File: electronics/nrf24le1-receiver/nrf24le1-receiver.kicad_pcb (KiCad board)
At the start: 2 copper layers, 16 parts, among them K1 CONN_3, K2 CONN_3, K3 CONN_3, K4 CONN_3, SW1 SW_PUSH, U1 MCP1703T-3302E/CB, U2 NRF24LE1-MODULE-15X21

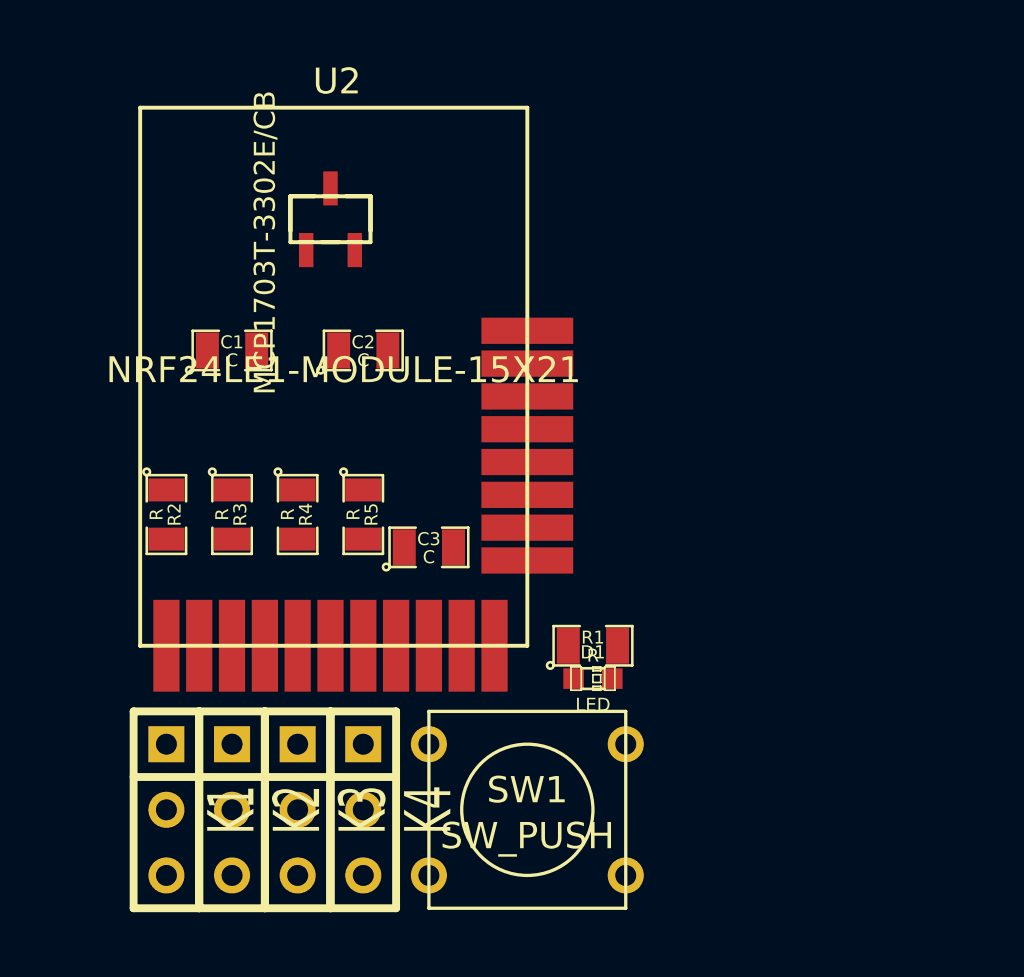
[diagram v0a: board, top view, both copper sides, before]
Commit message: Work on the layout of the NRF24LE1 receiver
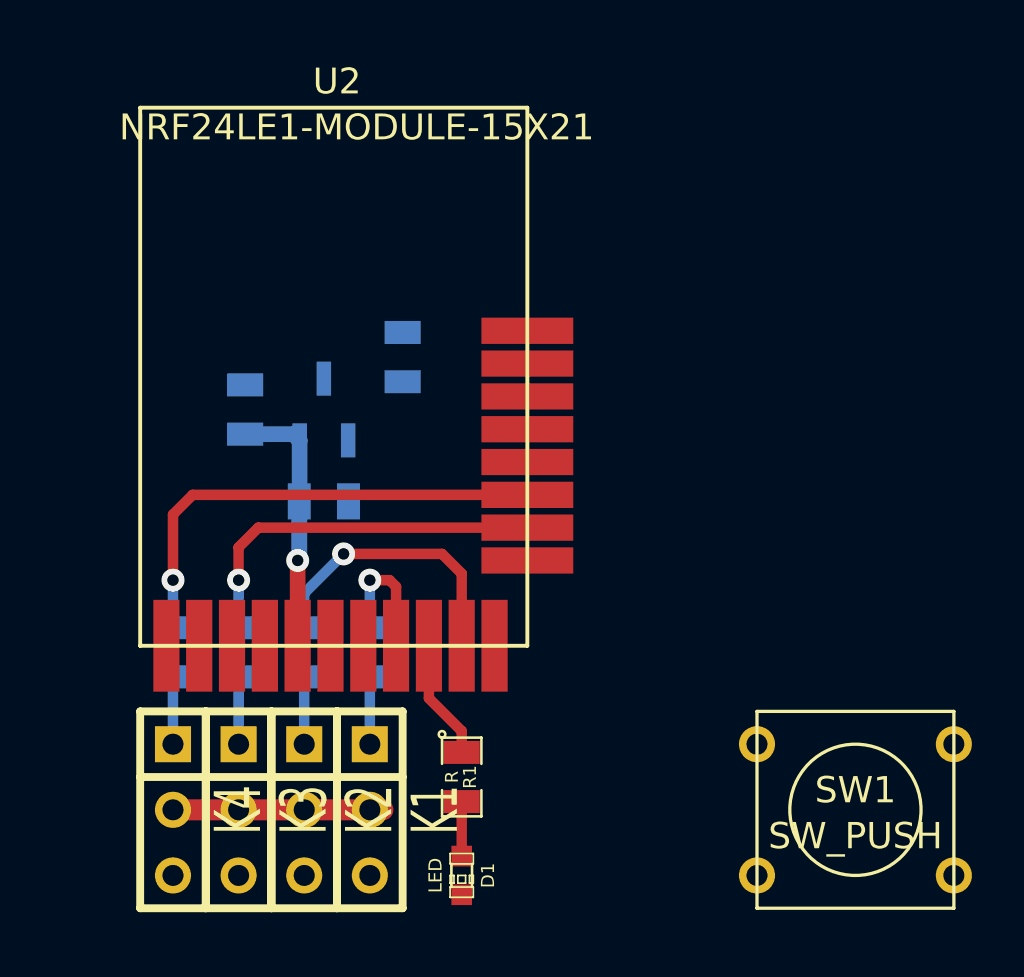
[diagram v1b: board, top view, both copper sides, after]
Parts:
- C1, C2, C3, R2, R3, R4, R5, U1: moved to B.Cu
- moved SW1 12.7 mm to (61.0, 68.6)
- moved R2 9.51 mm to (42.2, 62.5)
- moved D1 9.16 mm to (45.7, 71.1), turned to 270 degrees
- moved R5 9.09 mm to (34.5, 62.5)
- moved K1 7.87 mm to (42.2, 68.6)
- moved U1 7.37 mm to (40.4, 53.1), turned to 180 degrees
- moved K4 7.37 mm to (34.5, 68.6)
- moved R1 7.18 mm to (45.7, 67.3), turned to 270 degrees
- moved R3 6.02 mm to (39.6, 62.5)
- moved R4 5.80 mm to (37.1, 62.5)
- moved C3 4.44 mm to (40.4, 56.6)
- moved K2 2.79 mm to (39.6, 68.6)
- moved C1 2.34 mm to (37.3, 53.1), turned to 90 degrees
- moved K3 2.29 mm to (37.1, 68.6)
- moved C2 1.55 mm to (43.4, 51.1), turned to 90 degrees
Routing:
- net /MISO: track 0.00 -> 18.4 mm, vias 0 -> 1
- net /MOSI: track 0.00 -> 14.6 mm, vias 0 -> 1
- net /SCK: track 0.00 -> 11.2 mm, vias 0 -> 1
- net +3.3V: track 0.00 -> 10.2 mm, vias 0 -> 1
- net +BATT: track 0.00 -> 7.62 mm
- net /TX: track 0.00 -> 5.25 mm, vias 0 -> 1
- net /LED: track 0.00 -> 4.65 mm
- net N-0000017: track 0.00 -> 2.60 mm
- net N-0000016: track 0.00 -> 2.60 mm
- net N-0000015: track 0.00 -> 2.60 mm
- net N-0000014: track 0.00 -> 2.60 mm
- net N-000009: track 0.00 -> 2.11 mm
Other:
- net class Default: via_drill 0.635 -> 0.5
- rule trace_min: 0.254 -> 0.1524
- rule via_min_drill: 0.508 -> 0.3048
- rule via_min_size: 0.889 -> 0.6096

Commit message: Tweak schematics and layout
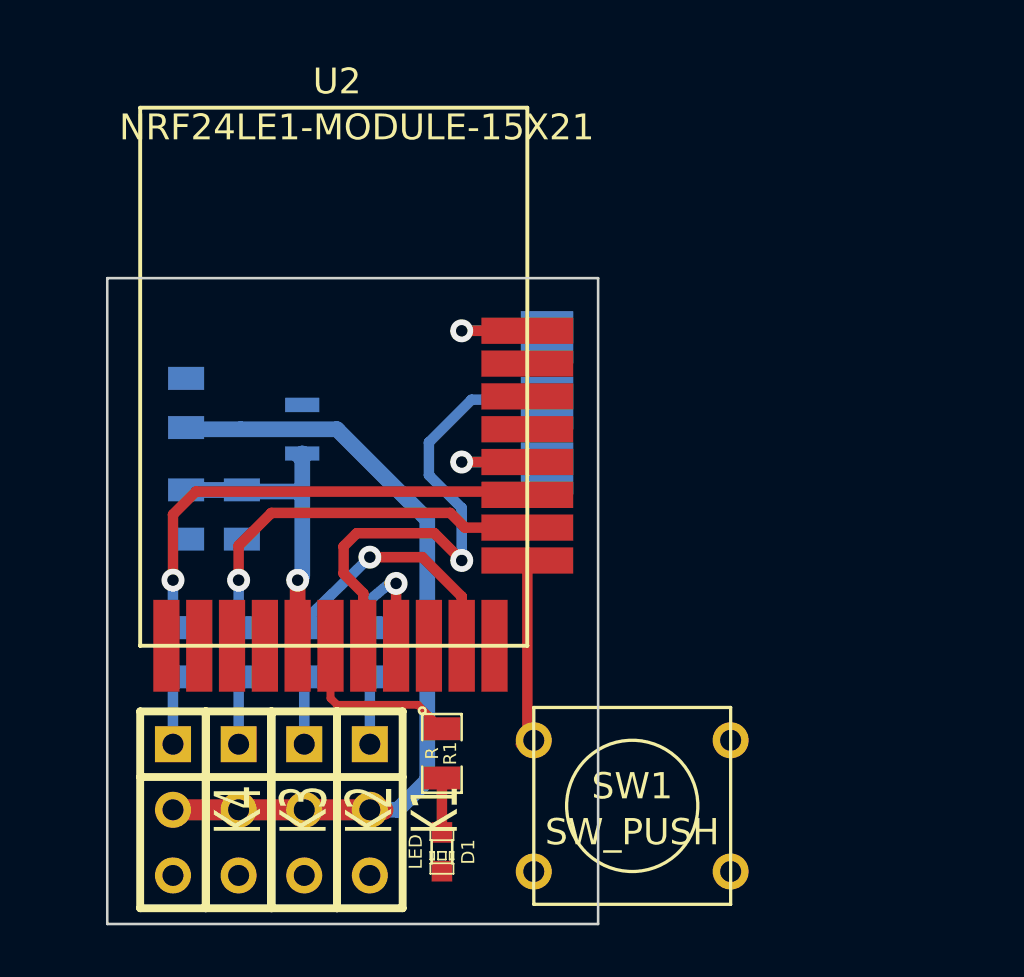
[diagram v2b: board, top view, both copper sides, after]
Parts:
- added P1: CONN_1, testpad_80mil_sq, B.Cu at (49.0, 52.8)
- added P2: CONN_1, testpad_80mil_sq, B.Cu at (49.0, 50.3)
- added P3: CONN_1, testpad_80mil_sq, B.Cu at (49.0, 55.4)
- moved SW1 8.64 mm to (52.3, 68.4)
- moved C2 8.57 mm to (35.1, 52.8)
- moved C1 4.66 mm to (35.1, 57.1), turned to 270 degrees
- moved C3 3.22 mm to (37.2, 57.1), turned to 270 degrees
- moved U1 2.17 mm to (38.4, 53.8), turned to 270 degrees
- moved D1 1.19 mm to (45.0, 70.2)
- moved R1 1.19 mm to (45.0, 66.4)
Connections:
- net /MISO renamed /CH1-MISO
- net /MOSI renamed /CH2-MOSI
- net /SCK renamed /CH3-SCK
- U2 pad 15: (no net) -> /CSN
- U2 pad 19: (no net) -> /RESET
- U2 pad 6: (no net) -> /LED
- U2 pad 7: (no net) -> /PROG
- U2 pad 9: /LED -> (no net)
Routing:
- net +BATT: track 7.62 -> 31.2 mm
- net /PROG: track 0.00 -> 19.0 mm, vias 0 -> 1
- net /BIND: track 0.00 -> 7.22 mm
- net /RESET: track 0.00 -> 5.13 mm, vias 0 -> 1
- net /CSN: track 0.00 -> 5.13 mm, vias 0 -> 1
- net /LED: track 4.65 -> 6.84 mm
- net +3.3V: track 10.2 -> 12.2 mm
- net /CH3-SCK: track 11.2 -> 9.89 mm
- net /CH2-MOSI: track 14.6 -> 15.1 mm
- added copper zone on B.Cu, net VSS
- added copper zone on F.Cu, net VSS
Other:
- board outline added: 19 x 25 mm

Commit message: Use round tact switch, tidy up the board
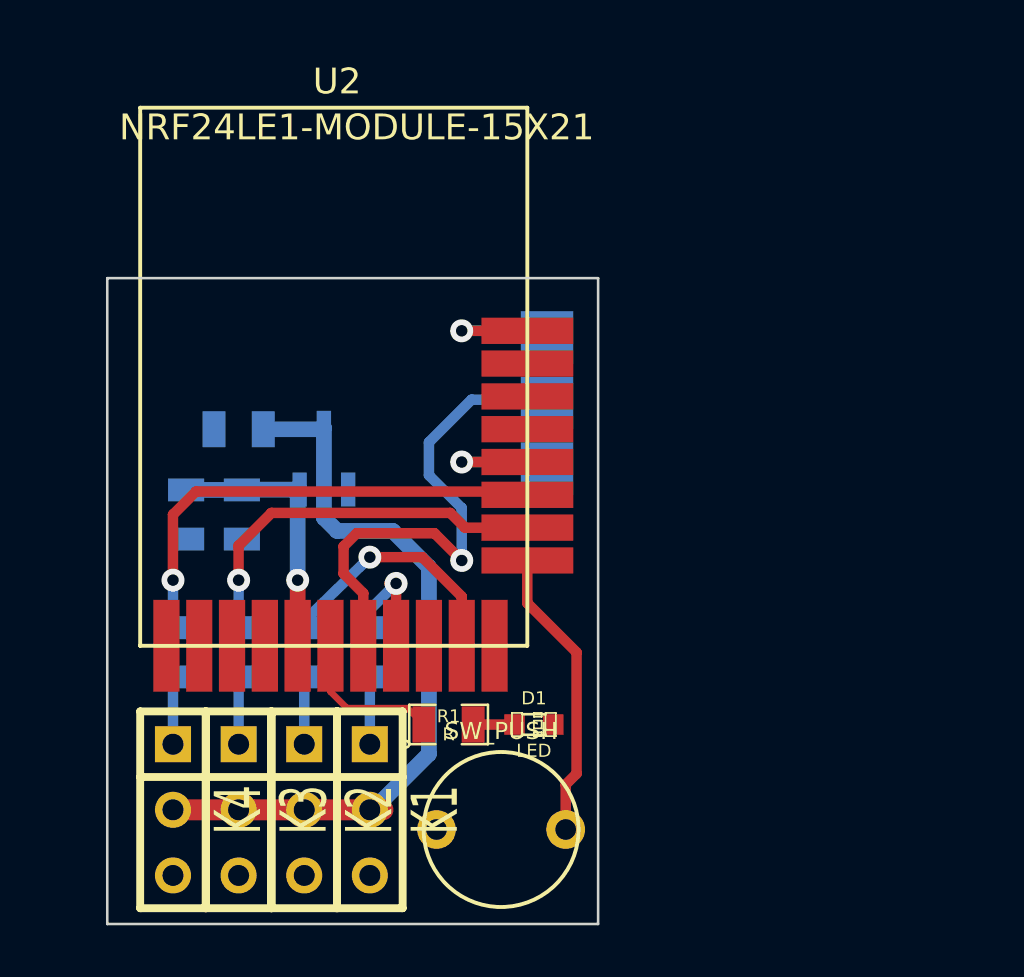
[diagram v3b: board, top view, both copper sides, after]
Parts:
- SW1: footprint SW_PUSH_SMALL -> SW_PUSH_ROUND_6mm
- moved D1 6.08 mm to (48.5, 65.3), turned to 0 degrees
- moved SW1 5.16 mm to (47.2, 69.3), turned to 180 degrees
- moved U1 2.33 mm to (40.4, 55.0), turned to 180 degrees
- moved C2 2.27 mm to (37.1, 53.8), turned to 180 degrees
- moved R1 1.15 mm to (45.2, 65.3), turned to 0 degrees
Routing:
- net /BIND: track 7.22 -> 11.4 mm
- net +BATT: track 31.2 -> 28.7 mm
- net +3.3V: track 12.2 -> 10.6 mm
- net /LED: track 6.84 -> 5.92 mm
- net N-000003: track 2.11 -> 1.60 mm

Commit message: Improve silk screen
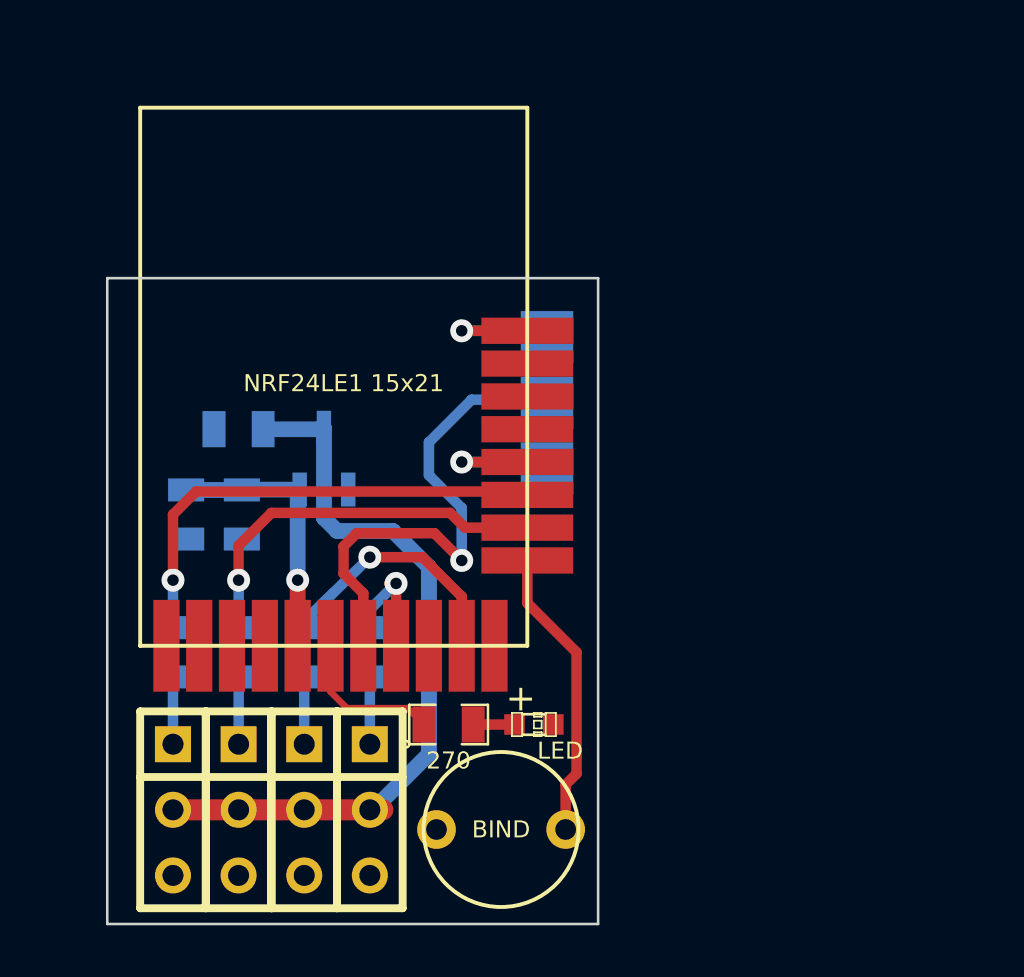
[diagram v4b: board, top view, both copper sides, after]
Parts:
- C1: value C -> 10u
- C2, C3: value C -> 1u
- R1: value R -> 270
- R2, R3, R4, R5: value R -> 820
- SW1: value SW_PUSH -> BIND
- U1: value MCP1703T-3302E/CB -> MCP1703
- U2: value NRF24LE1-MODULE-15X21 -> NRF24LE1 15x21
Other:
- board text added: "+"
- board text added: "CSN"
- board text added: "LANE Boys RC"
- board text added: "MISO"
- board text added: "MOSI"
- board text added: "NRF24LE1 receiver"
- board text added: "PROG"
- board text added: "RESET"
- board text added: "Rev 1"
- board text added: "SCK"
- board text added: "TX"

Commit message: Make pinout similar to XR3100
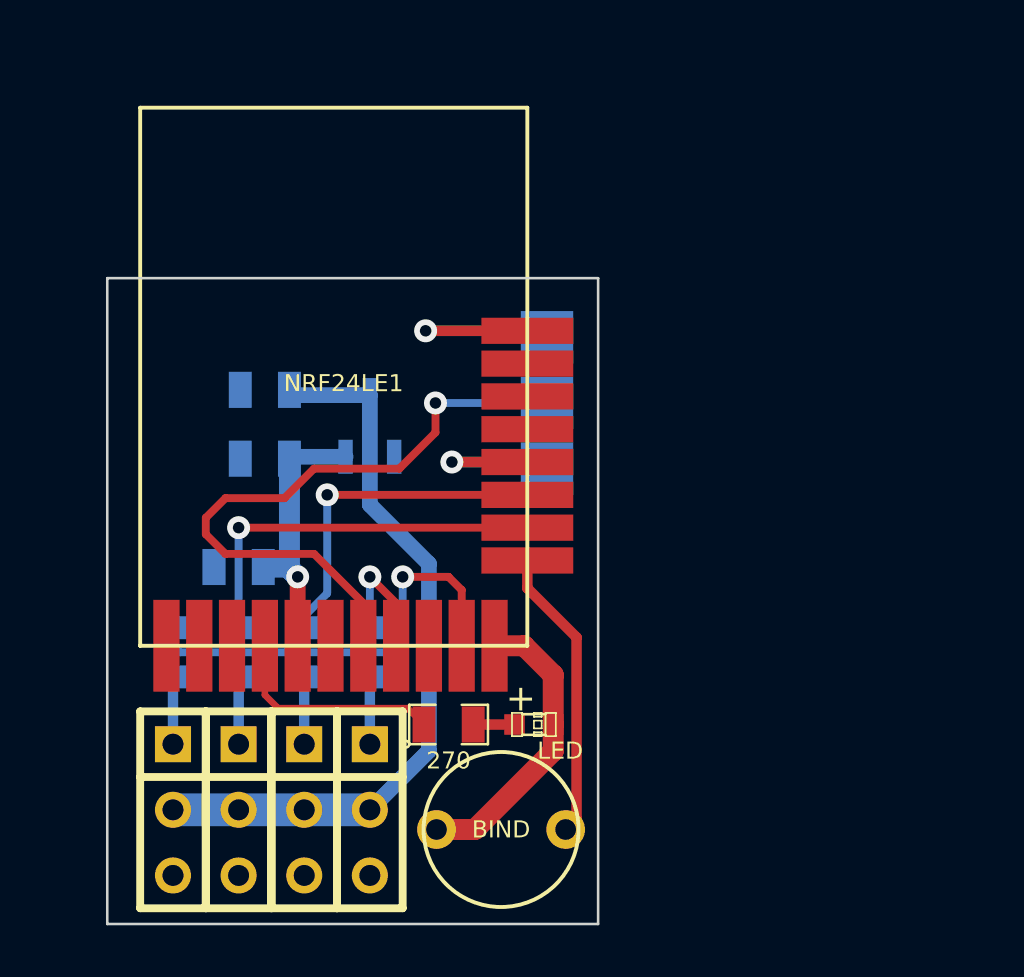
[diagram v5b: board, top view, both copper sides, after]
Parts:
- U2: value NRF24LE1 15x21 -> NRF24LE1
- moved C1 2.87 mm to (37.1, 59.2), turned to 180 degrees
- moved C3 2.33 mm to (38.1, 55.0), turned to 180 degrees
- moved U1 2.18 mm to (42.2, 53.7)
- moved C2 1.83 mm to (38.1, 52.3)
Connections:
- R3 pad 1: /CH3-SCK -> /CH3-MISO
- R5 pad 1: /CH1-MISO -> /CH1-SCK
- U2 pad 10: /CH3-SCK -> /CH1-SCK
- U2 pad 14: /CH1-MISO -> /CH3-MISO
- U2 pad 4: (no net) -> /LED
- U2 pad 6: /LED -> (no net)
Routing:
- net /CH1-MISO: track 18.5 -> 0.00 mm, vias 1 -> 0
- net /CH1-SCK: track 0.00 -> 17.1 mm, vias 0 -> 1
- net /CH3-MISO: track 0.00 -> 13.3 mm, vias 0 -> 1
- net VSS: track 0.00 -> 11.5 mm
- net /CH3-SCK: track 9.89 -> 0.00 mm, vias 1 -> 0
- net /PROG: track 19.0 -> 25.2 mm
- net /RESET: track 5.13 -> 7.93 mm
- net /LED: track 5.92 -> 8.54 mm
- net /CSN: track 5.13 -> 5.89 mm
- net +3.3V: track 10.6 -> 11.1 mm

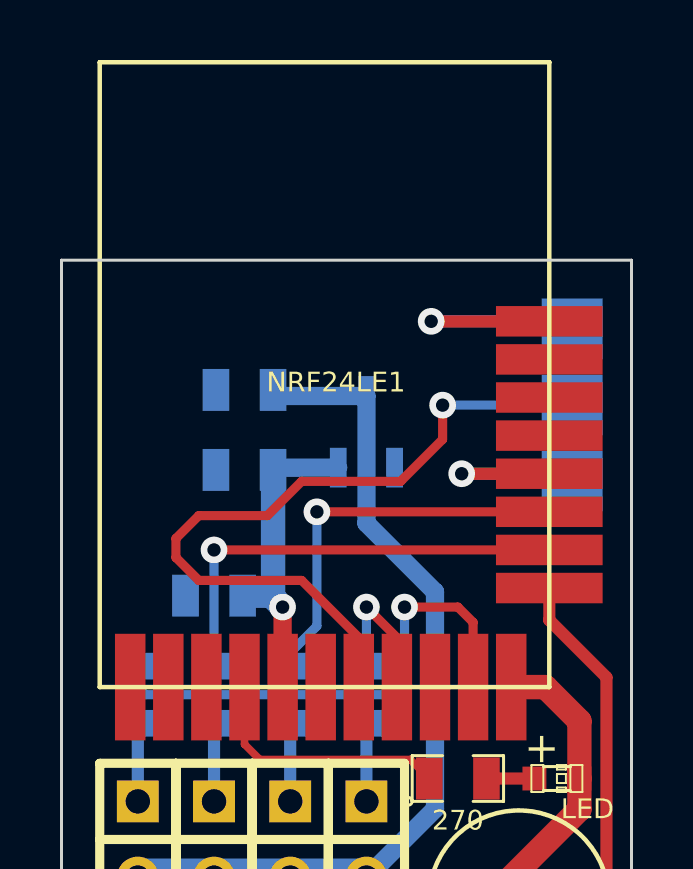
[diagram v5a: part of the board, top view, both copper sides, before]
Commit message: Finalize boards and make combined Gerbers for manufacturing
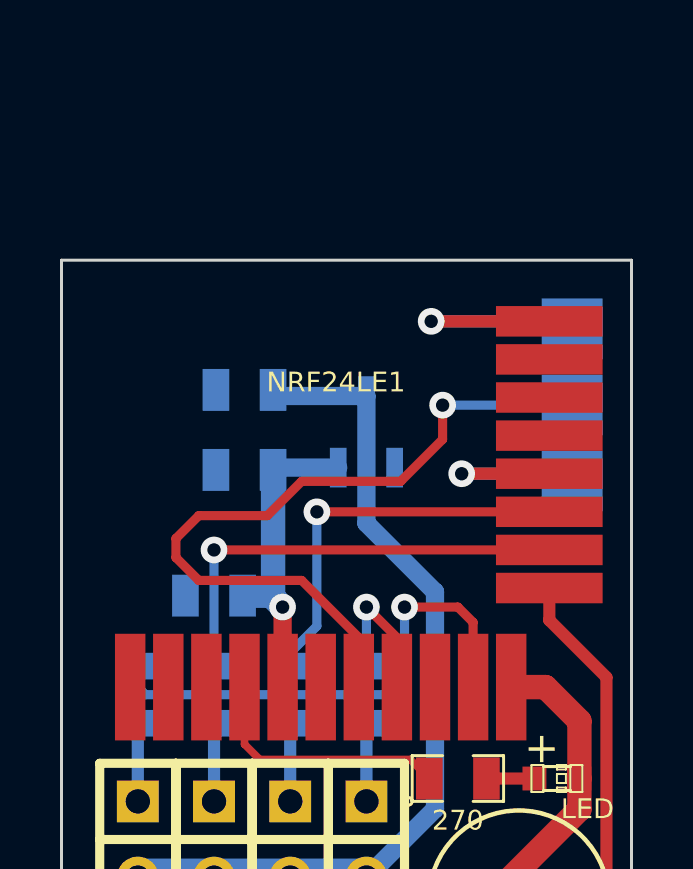
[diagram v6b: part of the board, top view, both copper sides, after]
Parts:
- R2, R3, R4, R5: value 820 -> 680
